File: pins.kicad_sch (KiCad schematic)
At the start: 0 parts

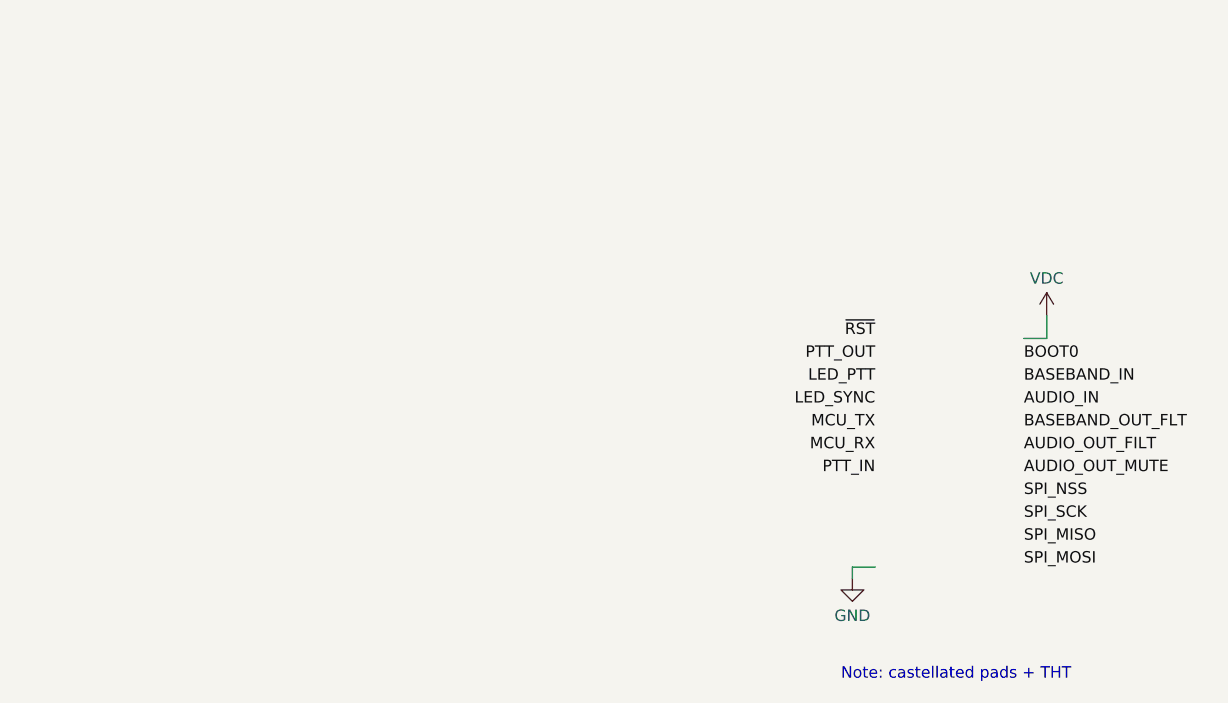
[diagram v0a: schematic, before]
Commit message: First Edits
Added J1 connector, finished filters and swapped µC to STM32G473
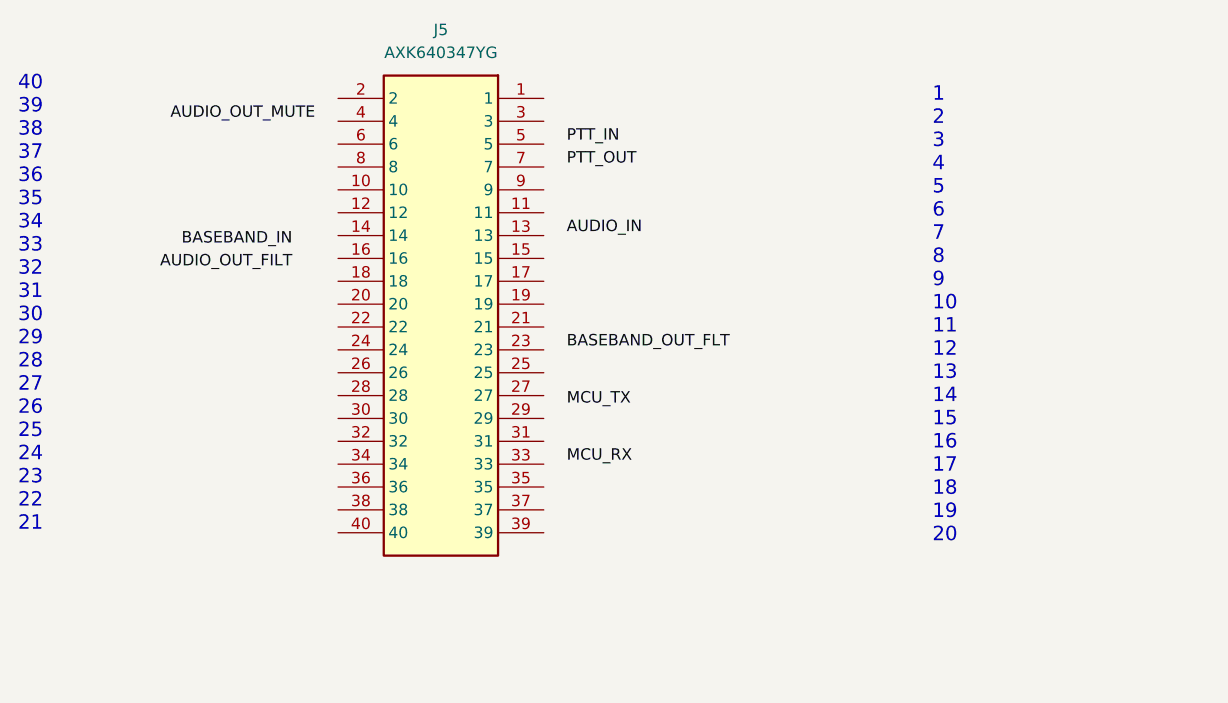
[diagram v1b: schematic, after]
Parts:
- added J5: AXK640347YG, AXK640347YG:AXK640347YG, symbol AXK640347YG:AXK640347YG
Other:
- note added: "1 2 3 4 5 6 7 8 9 10 11 12 13 14 15 16 17 18 19 20"
- note added: "40 39 38 37 36 35 34 33 32 31 30 29 28 27 26 25 24 23 22 21"
- note removed: "Note: castellated pads + THT"
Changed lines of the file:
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@@
     (comment 1 "M17 Project, OpenRTX")
   )
-  (wire (pts (xy 153.67 78.74) (xy 156.21 78.74))
-    (stroke (width 0) (type default))
+  (text "40\n39\n38\n37\n36\n35\n34\n33\n32\n31\n30\n29\n28\n27\n26\n25\n24\n23\n22\n21"
+    (at 41.91 100.33 0)
+    (effects (font (size 1.6 1.6)) (justify left bottom))
   )
-  (wire (pts (xy 134.62 105.41) (xy 134.62 104.14))
-    (stroke (width 0) (type default))
+  (text "1\n2\n3\n4\n5\n6\n7\n8\n9\n10\n11\n12\n13\n14\n15\n16\n17\n18\n19\n20"
+    (at 143.51 101.6 0)
+    (effects (font (size 1.6 1.6)) (justify left bottom))
   )
-  (wire (pts (xy 134.62 104.14) (xy 137.16 104.14))
-    (stroke (width 0) (type default))
-  )
-  (wire (pts (xy 156.21 78.74) (xy 156.21 76.2))
-    (stroke (width 0) (type default))
-  )
-  (text "Note: castellated pads + THT" (at 133.35 116.84 0)
+  (label "PTT_IN" (at 102.87 57.15 0) (fields_autoplaced)
     (effects (font (size 1.27 1.27)) (justify left bottom))
   )
-  (label "LED_PTT" (at 137.16 83.82 180) (fields_autoplaced)
+  (label "PTT_OUT" (at 102.87 59.69 0) (fields_autoplaced)
+    (effects (font (size 1.27 1.27)) (justify left bottom))
+  )
+  (label "BASEBAND_IN" (at 72.39 68.58 180) (fields_autoplaced)
     (effects (font (size 1.27 1.27)) (justify right bottom))
   )
-  (label "SPI_MISO" (at 153.67 101.6 0) (fields_autoplaced)
+  (label "AUDIO_IN" (at 102.87 67.31 0) (fields_autoplaced)
     (effects (font (size 1.27 1.27)) (justify left bottom))
   )
-  (label "PTT_IN" (at 137.16 93.98 180) (fields_autoplaced)
+  (label "BASEBAND_OUT_FLT" (at 102.87 80.01 0) (fields_autoplaced)
+    (effects (font (size 1.27 1.27)) (justify left bottom))
+  )
+  (label "MCU_TX" (at 102.87 86.36 0) (fields_autoplaced)
+    (effects (font (size 1.27 1.27)) (justify left bottom))
+  )
+  (label "MCU_RX" (at 102.87 92.71 0) (fields_autoplaced)
+    (effects (font (size 1.27 1.27)) (justify left bottom))
+  )
+  (label "AUDIO_OUT_FILT" (at 72.39 71.12 180) (fields_autoplaced)
     (effects (font (size 1.27 1.27)) (justify right bottom))
   )
-  (label "PTT_OUT" (at 137.16 81.28 180) (fields_autoplaced)
+  (label "AUDIO_OUT_MUTE" (at 74.93 54.61 180) (fields_autoplaced)
     (effects (font (size 1.27 1.27)) (justify right bottom))
   )
-  (label "BASEBAND_IN" (at 153.67 83.82 0) (fields_autoplaced)
-    (effects (font (size 1.27 1.27)) (justify left bottom))
-  )
-  (label "AUDIO_IN" (at 153.67 86.36 0) (fields_autoplaced)
-    (effects (font (size 1.27 1.27)) (justify left bottom))
-  )
-  (label "BASEBAND_OUT_FLT" (at 153.67 88.9 0) (fields_autoplaced)
-    (effects (font (size 1.27 1.27)) (justify left bottom))
-  )
-  (label "SPI_SCK" (at 153.67 99.06 0) (fields_autoplaced)
-    (effects (font (size 1.27 1.27)) (justify left bottom))
-  )
-  (label "MCU_TX" (at 137.16 88.9 180) (fields_autoplaced)
-    (effects (font (size 1.27 1.27)) (justify right bottom))
-  )
-  (label "SPI_MOSI" (at 153.67 104.14 0) (fields_autoplaced)
-    (effects (font (size 1.27 1.27)) (justify left bottom))
-  )
-  (label "LED_SYNC" (at 137.16 86.36 180) (fields_autoplaced)
-    (effects (font (size 1.27 1.27)) (justify right bottom))
-  )
-  (label "SPI_NSS" (at 153.67 96.52 0) (fields_autoplaced)
-    (effects (font (size 1.27 1.27)) (justify left bottom))
-  )
-  (label "MCU_RX" (at 137.16 91.44 180) (fields_autoplaced)
-    (effects (font (size 1.27 1.27)) (justify right bottom))
-  )
-  (label "AUDIO_OUT_FILT" (at 153.67 91.44 0) (fields_autoplaced)
-    (effects (font (size 1.27 1.27)) (justify left bottom))
-  )
-  (label "BOOT0" (at 153.67 81.28 0) (fields_autoplaced)
-    (effects (font (size 1.27 1.27)) (justify left bottom))
-  )
-  (label "~{RST}" (at 137.16 78.74 180) (fields_autoplaced)
-    (effects (font (size 1.27 1.27)) (justify right bottom))
-  )
-  (label "AUDIO_OUT_MUTE" (at 153.67 93.98 0) (fields_autoplaced)
-    (effects (font (size 1.27 1.27)) (justify left bottom))
-  )
-  (symbol (lib_id "power:GND") (at 134.62 105.41 0) (unit 1)
-    (in_bom yes) (on_board yes) (dnp no) (fields_autoplaced)
-    (property "Reference" "#PWR042" (at 134.62 111.76 0)
-      (effects (font (size 1.27 1.27)) hide)
-    )
-    (property "Value" "GND" (at 134.62 109.5431 0)
+  (symbol (lib_id "AXK640347YG:AXK640347YG") (at 100.33 52.07 0) (mirror y) (unit 1)
+    (in_bom yes) (on_board yes) (dnp no)
+    (property "Reference" "J5" (at 88.9 44.45 0)
       (effects (font (size 1.27 1.27)))
     )
-    (property "Footprint" "" (at 134.62 105.41 0)
-      (effects (font (size 1.27 1.27)) hide)
+    (property "Value" "AXK640347YG" (at 88.9 46.99 0)
+      (effects (font (size 1.27 1.27)))
     )
-    (property "Datasheet" "" (at 134.62 105.41 0)
-      (effects (font (size 1.27 1.27)) hide)
+    (property "Footprint" "AXK640347YG:AXK640347YG" (at 81.28 146.99 0)
+      (effects (font (size 1.27 1.27)) (justify left top) hide)
+    )
+    (property "Datasheet" "https://componentsearchengine.com/Datasheets/1/AXK640347YG.pdf" (at 81.28 246.99 0)
+      (effects (font (size 1.27 1.27)) (justify left top) hide)
+    )
+    (property "Height" "2.6" (at 81.28 446.99 0)
+      (effects (font (size 1.27 1.27)) (justify left top) hide)
+    )
+    (property "Mouser Part Number" "769-AXK640347YG" (at 81.28 546.99 0)
+      (effects (font (size 1.27 1.27)) (justify left top) hide)
+    )
+    (property "Mouser Price/Stock" "https://www.mouser.com/Search/Refine.aspx?Keyword=769-AXK640347YG" (at 81.28 646.99 0)
+      (effects (font (size 1.27 1.27)) (justify left top) hide)
+    )
+    (property "Manufacturer_Name" "Panasonic" (at 81.28 746.99 0)
+      (effects (font (size 1.27 1.27)) (justify left top) hide)
+    )
+    (property "Manufacturer_Part_Number" "AXK640347YG" (at 81.28 846.99 0)
+      (effects (font (size 1.27 1.27)) (justify left top) hide)
     )
     (pin "1")
+    (pin "11")
+    (pin "33")
+    (pin "13")
+    (pin "17")
+    (pin "27")
+    (pin "29")
+    (pin "37")
+    (pin "19")
+    (pin "15")
+    (pin "36")
+    (pin "3")
+    (pin "24")
+    (pin "32")
+    (pin "30")
+    (pin "6")
+    (pin "31")
+    (pin "14")
+    (pin "35")
+    (pin "9")
+    (pin "8")
+    (pin "28")
+    (pin "5")
+    (pin "34")
+    (pin "7")
+    (pin "2")
+    (pin "40")
+    (pin "20")
+    (pin "4")
+    (pin "38")
+    (pin "22")
+    (pin "39")
+    (pin "21")
+    (pin "16")
+    (pin "23")
+    (pin "26")
+    (pin "25")
+    (pin "18")
+    (pin "12")
+    (pin "10")
     (instances
       (project "micro17"
-        (path "/8b0d7f56-1962-40c9-8b95-6d4fe558acbc"
-          (reference "#PWR042") (unit 1)
-        )
         (path "/8b0d7f56-1962-40c9-8b95-6d4fe558acbc/13b6b83b-ed33-487f-9920-ee485cde78f6"
-          (reference "#PWR048") (unit 1)
+          (reference "J5") (unit 1)
         )
       )
-    )
-  )
-  (symbol (lib_id "power:VDC") (at 156.21 76.2 0) (unit 1)
-    (in_bom yes) (on_board yes) (dnp no) (fields_autoplaced)
-    (property "Reference" "#PWR043" (at 156.21 78.74 0)
-      (effects (font (size 1.27 1.27)) hide)
-    )
-    (property "Value" "VDC" (at 156.21 72.0669 0)
-      (effects (font (size 1.27 1.27)))
-    )
-    (property "Footprint" "" (at 156.21 76.2 0)
-      (effects (font (size 1.27 1.27)) hide)
-    )
-    (property "Datasheet" "" (at 156.21 76.2 0)
-      (effects (font (size 1.27 1.27)) hide)
-    )
-    (pin "1")
-    (instances
-      (project "micro17"
-        (path "/8b0d7f56-1962-40c9-8b95-6d4fe558acbc"
-          (reference "#PWR043") (unit 1)
-        )
-        (path "/8b0d7f56-1962-40c9-8b95-6d4fe558acbc/13b6b83b-ed33-487f-9920-ee485cde78f6"
-          (reference "#PWR049") (unit 1)
-        )
-      )

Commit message: PCB routed, gerbers and ibom included
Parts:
- removed J5: AXK640347YG, AXK640347YG:AXK640347YG, symbol AXK640347YG:AXK640347YG
- added FB1: FerriteBead_Small, Capacitor_SMD:C_0603_1608Metric, symbol Device:FerriteBead_Small
- added J5: AXK640347YG, Micro17-ICOM_Board:AXK640347YG, symbol Connector_Generic:Conn_02x20_Counter_Clockwise
- added J6: Conn_01x40_Pin, Connector_FFC-FPC:Hirose_FH12-40S-0.5SH_1x40-1MP_P0.50mm_Horizontal, symbol Connector:Conn_01x40_Pin
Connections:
- net AUDIO_IN: now also J5.7 (Pin_7)
- net AUDIO_OUT_FILT: now also J5.30 (Pin_30)
- net AUDIO_OUT_MUTE: now also J5.34 (Pin_34)
- net BASEBAND_IN: now also J5.31 (Pin_31)
- net MCU_RX: now also J5.14 (Pin_14)
- net MCU_TX: now also J5.15 (Pin_15)
- net PTT_IN: now also J5.3 (Pin_3)
- net PTT_OUT: now also J5.4 (Pin_4)
- new net: FB1.2, J5.38 (Pin_38)
- new net +5V: FB1.1
- new net +5VD: J6.19 (Pin_19), J6.37 (Pin_37)
- new net 13V2: J6.5 (Pin_5)
- new net BASEBAND_OUT_FILT: J5.13 (Pin_13)
- new net BUS+: J6.6 (Pin_6)
- new net CH_Activity: J6.8 (Pin_8)
- new net DISCAUDIO: J6.7 (Pin_7)
- new net GND: J5.17 (Pin_17), J5.2 (Pin_2), J5.39 (Pin_39), J6.1 (Pin_1)
- new net OPT_CS: J6.30 (Pin_30)
- new net RDY: J6.29 (Pin_29)
- no-connect marks 0 -> 27
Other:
- note added: "GM360 J0551"
- note added: "Microphone"

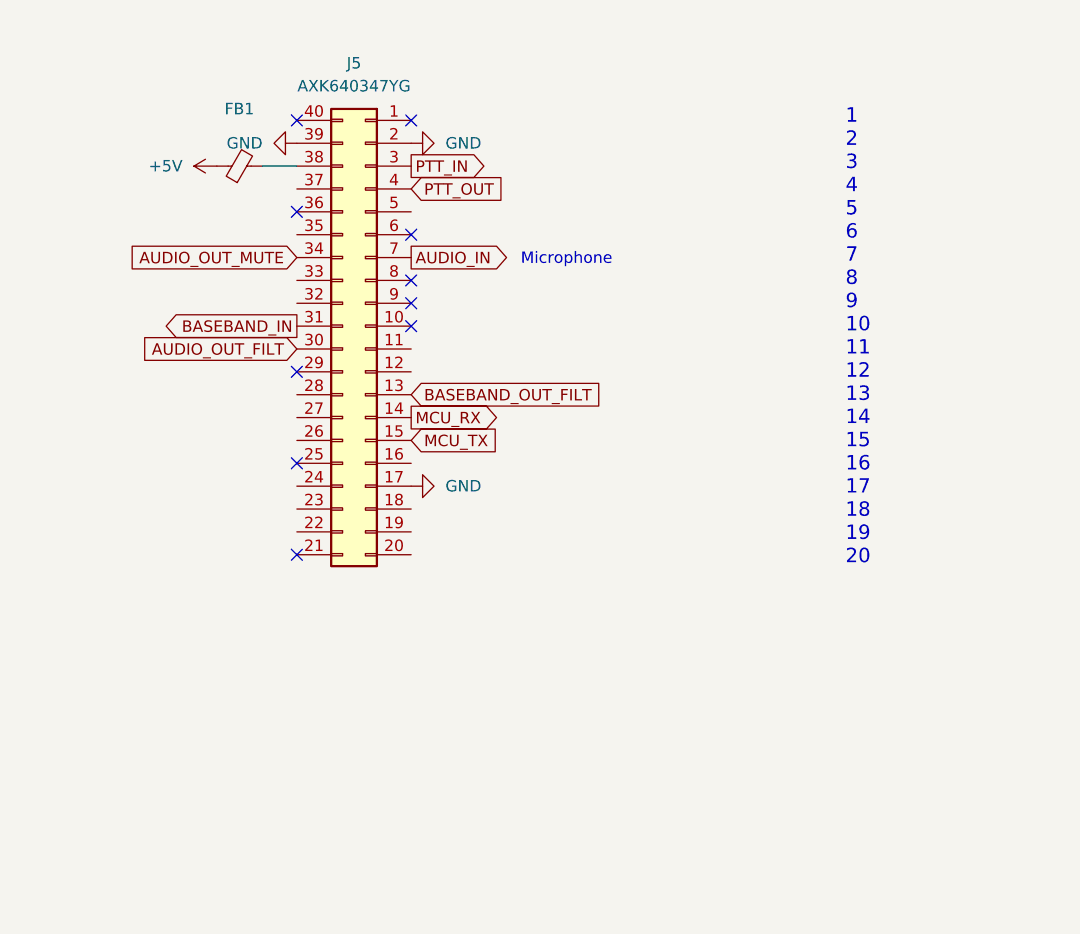
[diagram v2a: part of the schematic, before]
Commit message: Updates
GP relay added,
3v3 added to programming conn.
diode(dnp) added for motorola type internal bus.
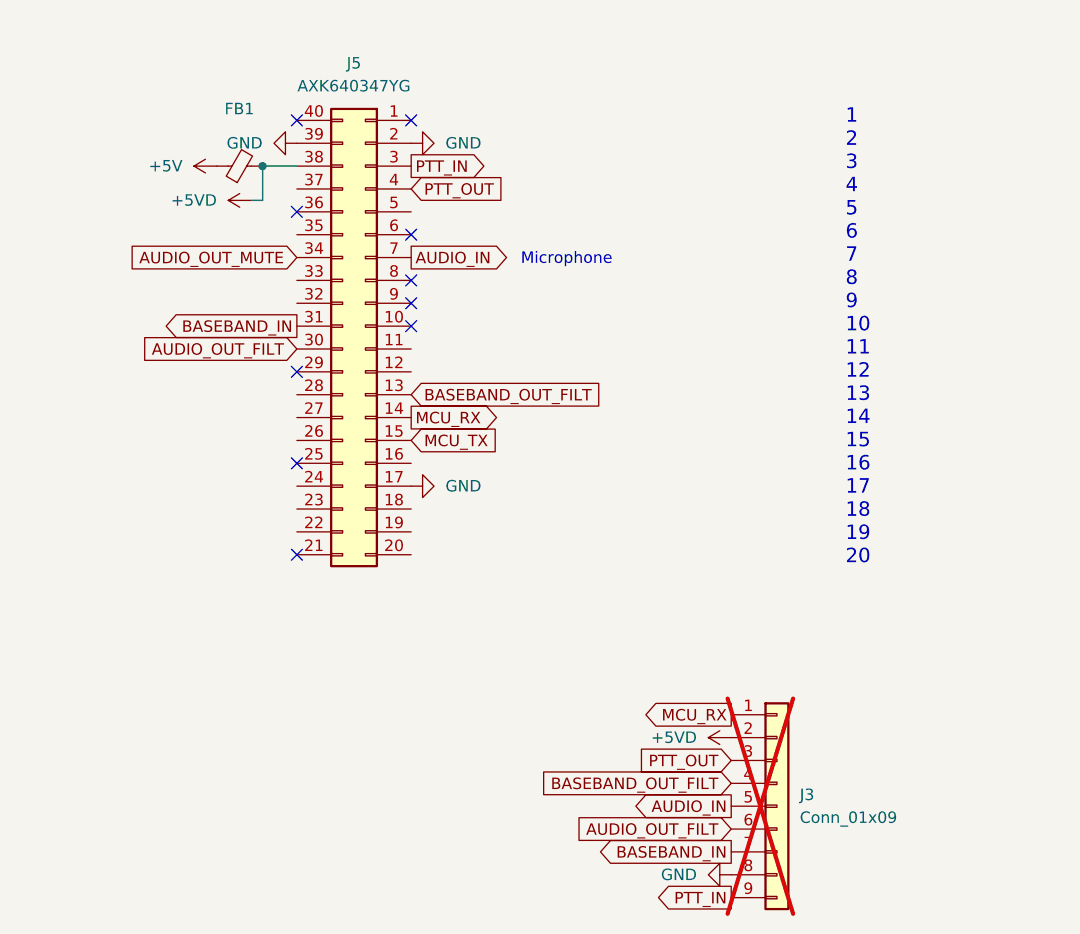
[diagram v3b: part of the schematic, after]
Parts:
- added J3: Conn_01x09, Connector_PinSocket_2.00mm:PinSocket_1x09_P2.00mm_Horizontal, symbol Connector_Generic:Conn_01x09
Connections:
- net +5VD: now also FB1.2, J5.38 (Pin_38), J3.2 (Pin_2)
- net AUDIO_IN: now also J3.5 (Pin_5)
- net AUDIO_OUT_FILT: now also J3.6 (Pin_6)
- net BASEBAND_IN: now also J3.7 (Pin_7)
- net BASEBAND_OUT_FILT: now also J3.4 (Pin_4)
- net GND: now also J3.8 (Pin_8)
- net MCU_RX: now also J3.1 (Pin_1)
- net PTT_IN: now also J3.9 (Pin_9)
- net PTT_OUT: now also J3.3 (Pin_3)

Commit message: LCSC part numbers included into schematics
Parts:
- FB1: LCSC (none) -> C2971885
- J5: LCSC (none) -> C2936870
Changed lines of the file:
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@@
+			)
+		)
+		(property "Height" ""
+			(at 135.89 128.27 0)
+			(effects
+				(font
+					(size 1.27 1.27)
+				)
+				(hide yes)
+			)
+		)
+		(property "Manufacturer_Name" ""
+			(at 135.89 128.27 0)
+			(effects
+				(font
+					(size 1.27 1.27)
+				)
+				(hide yes)
+			)
+		)
+		(property "Manufacturer_Part_Number" ""
+			(at 135.89 128.27 0)
+			(effects
+				(font
+					(size 1.27 1.27)
+				)
+				(hide yes)
+			)
+		)
+		(property "Mouser Part Number" ""
+			(at 135.89 128.27 0)
+			(effects
+				(font
+					(size 1.27 1.27)
+				)
+				(hide yes)
+			)
+		)
+		(property "Mouser Price/Stock" ""
+			(at 135.89 128.27 0)
+			(effects
+				(font
+					(size 1.27 1.27)
+				)
+				(hide yes)
+			)
+		)
+		(property "JLC" ""
+			(at 135.89 128.27 0)
+			(effects
+				(font
+					(size 1.27 1.27)
+				)
+				(hide yes)
 			)
 		)
@@
 			)
 		)
+		(property "Height" ""
+			(at 90.17 74.93 0)
+			(effects
+				(font
+					(size 1.27 1.27)
+				)
+				(hide yes)
+			)
+		)
+		(property "Manufacturer_Name" ""
+			(at 90.17 74.93 0)
+			(effects
+				(font
+					(size 1.27 1.27)
+				)
+				(hide yes)
+			)
+		)
+		(property "Manufacturer_Part_Number" ""
+			(at 90.17 74.93 0)
+			(effects
+				(font
+					(size 1.27 1.27)
+				)
+				(hide yes)
+			)
+		)
+		(property "Mouser Part Number" ""
+			(at 90.17 74.93 0)
+			(effects
+				(font
+					(size 1.27 1.27)
+				)
+				(hide yes)
+			)
+		)
+		(property "Mouser Price/Stock" ""
+			(at 90.17 74.93 0)
+			(effects
+				(font
+					(size 1.27 1.27)
+				)
+				(hide yes)
+			)
+		)
+		(property "LCSC" "C2936870"
+			(at 90.17 74.93 0)
+			(effects
+				(font
+					(size 1.27 1.27)
+				)
+				(hide yes)
+			)
+		)
+		(property "JLC" ""
+			(at 90.17 74.93 0)
+			(effects
+				(font
+					(size 1.27 1.27)
+				)
+				(hide yes)
+			)
+		)
 		(pin "33"
 		)
@@
 			)
 		)
+		(property "Height" ""
+			(at 224.79 78.74 0)
+			(effects
+				(font
+					(size 1.27 1.27)
+				)
+				(hide yes)
+			)
+		)
+		(property "Manufacturer_Name" ""
+			(at 224.79 78.74 0)
+			(effects
+				(font
+					(size 1.27 1.27)
+				)
+				(hide yes)
+			)
+		)
+		(property "Manufacturer_Part_Number" ""
+			(at 224.79 78.74 0)
+			(effects
+				(font
+					(size 1.27 1.27)
+				)
+				(hide yes)
+			)
+		)
+		(property "Mouser Part Number" ""
+			(at 224.79 78.74 0)
+			(effects
+				(font
+					(size 1.27 1.27)
+				)
+				(hide yes)
+			)
+		)
+		(property "Mouser Price/Stock" ""
+			(at 224.79 78.74 0)
+			(effects
+				(font
+					(size 1.27 1.27)
+				)
+				(hide yes)
+			)
+		)
+		(property "JLC" ""
+			(at 224.79 78.74 0)
+			(effects
+				(font
+					(size 1.27 1.27)
+				)
+				(hide yes)
+			)
+		)
 		(pin "35"
 		)
@@
 			(at 76.2 57.15 0)
 			(effects
+				(font
+					(size 1.27 1.27)
+				)
+				(hide yes)
+			)
+		)
+		(property "Height" ""
+			(at 76.2 57.15 0)
+			(effects
+				(font
+					(size 1.27 1.27)
+				)
+				(hide yes)
+			)
+		)
+		(property "Manufacturer_Name" ""
+			(at 76.2 57.15 0)
+			(effects
+				(font
+					(size 1.27 1.27)
+				)
+				(hide yes)
+			)
+		)
+		(property "Manufacturer_Part_Number" ""
+			(at 76.2 57.15 0)
+			(effects
+				(font
+					(size 1.27 1.27)
+				)
+				(hide yes)
+			)
+		)
+		(property "Mouser Part Number" ""
+			(at 76.2 57.15 0)
+			(effects
+				(font
+					(size 1.27 1.27)
+				)
+				(hide yes)
+			)
+		)
+		(property "Mouser Price/Stock" ""
+			(at 76.2 57.15 0)
+			(effects
+				(font
+					(size 1.27 1.27)
+				)
+				(hide yes)
+			)
+		)
+		(property "LCSC" "C2971885"
+			(at 76.2 57.15 0)
+			(effects
+				(font
+					(size 1.27 1.27)
+				)
+				(hide yes)
+			)
+		)
+		(property "JLC" ""
+			(at 76.2 57.15 0)
+			(effects
